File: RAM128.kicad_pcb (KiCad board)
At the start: 4 copper layers, 71.6 x 35.7 mm, 33 parts, among them J1 AppleIIBus, U1 621024, U10 74LS32, U11 74AHC1G126GW, U2 74HCT245, U3 74LS273, U4 74LS273, U5 74LS04, U6 74LS08, U7 74LS08, U8 74LS08, U9 74LS08

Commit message: Update docs
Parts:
- C1: renamed from C13; value 2u2 -> 10u
- C11: renamed from C1; value 2u2 -> 10u
- C12: renamed from C5; value 2u2 -> 10u
- U10: value 74LS32 -> 74HCT32
- U3, U4: value 74LS273 -> 74HCT273
- U5: value 74LS04 -> 74HCT04
- U6, U7, U8, U9: value 74LS08 -> 74HCT08
- renumbered C12 to C10, C3 to C2, C11 to C3, C2 to C4, C6 to C5, C7 to C6, C8 to C7, C9 to C8, C10 to C9, FID5 to FID1, FID1 to FID3, H5 to H1, H1 to H3
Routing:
- net GND: vias 153 -> 154

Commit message: More stitching
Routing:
- net /ENRD: track 39.0 -> 29.8 mm
- net /~RES~: track 68.4 -> 62.8 mm
- net Net-(U10-Pad8): track 27.3 -> 24.6 mm
- net Net-(U10-Pad10): track 42.7 -> 40.0 mm
- net Net-(U10-Pad11): track 15.0 -> 13.9 mm
- net /R~WE~: track 102.2 -> 101.4 mm
- net Net-(U10-Pad9): track 16.6 -> 16.0 mm
- net GND: track 70.3 -> 69.7 mm, vias 154 -> 169

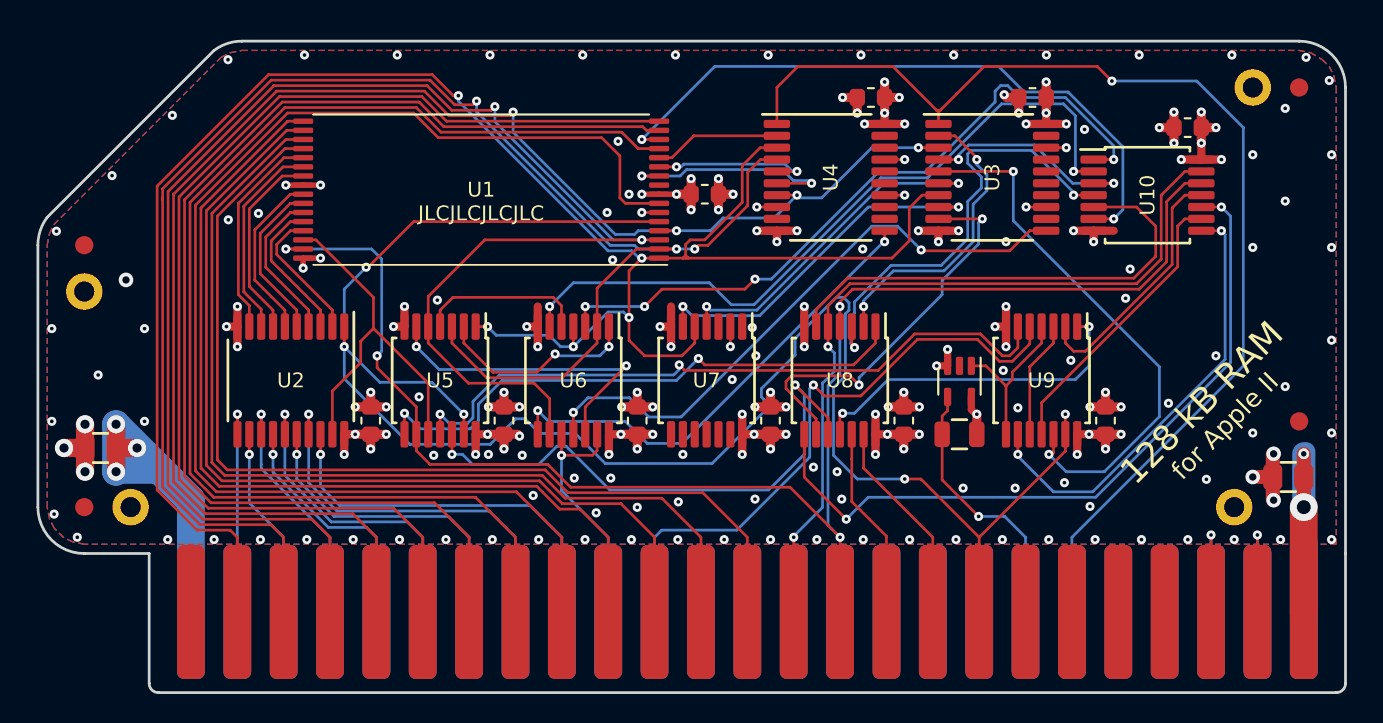
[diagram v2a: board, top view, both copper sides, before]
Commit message: Fixed clock bug
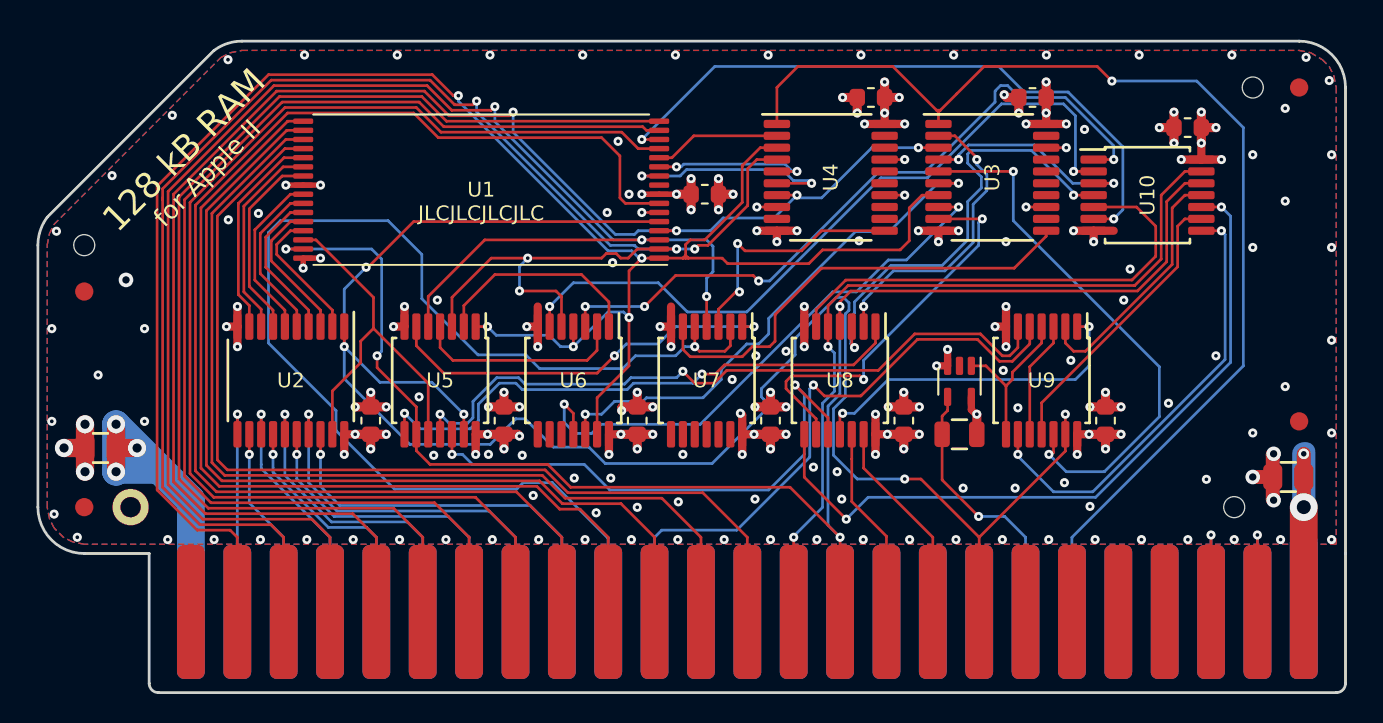
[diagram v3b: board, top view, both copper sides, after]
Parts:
- H2, H3, H4: footprint stdpads:PasteHole_1.1mm_PTH -> stdpads:PasteHole_1.152mm_NPTH
- U11: value 74AHC1G126GW -> 74AHCT1G126GW
- moved FID2 2.54 mm to (70.4, 117.7)
- moved H2 2.54 mm to (70.4, 115.2)
- turned U11 to 90 degrees
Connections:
- U6 pad 10: /~DEVSEL~ -> GND
- U6 pad 11: /~DEV~and~A2~ -> /ENWR1A0
- U6 pad 12: Net-(U5-Pad6) -> /ENWR1
- U6 pad 13: /~DEVSEL~ -> /A0
- U6 pad 2: /A1 -> Net-(U5-Pad4)
- U6 pad 5: Net-(U5-Pad4) -> /A1
- U6 pad 8: /~DEV~andA2 -> Net-(U6-Pad8)
- U6 pad 9: /A2 -> GND
- U7 pad 1: GND -> Net-(U5-Pad6)
- U7 pad 2: GND -> /~DEVSEL~
- U7 pad 3: Net-(U7-Pad3) -> /~DEV~andA2
- U7 pad 4: /ENWR1 -> /A2
- U7 pad 5: /A0 -> /~DEVSEL~
- U7 pad 6: /ENWR1A0 -> /~DEV~and~A2~
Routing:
- net /~DEVSEL~: track 13.7 -> 67.3 mm
- net /~DEV~andA2: track 26.2 -> 13.9 mm
- net /ENWR1A0: track 20.0 -> 31.0 mm
- net /ENWR1: track 19.0 -> 28.8 mm
- net /~DEV~and~A2~: track 33.2 -> 25.2 mm, vias 2 -> 0
- net Net-(U5-Pad6): track 17.9 -> 21.9 mm
- net /A1: track 90.5 -> 93.2 mm, vias 3 -> 5
- net Net-(U5-Pad4): track 9.18 -> 11.6 mm
- net /A2: track 89.2 -> 87.0 mm, vias 2 -> 3
- net /A0: track 108.7 -> 109.7 mm
- net GND: track 69.7 -> 68.8 mm, vias 169 -> 168
- net Net-(U5-Pad12): track 30.3 -> 29.5 mm
- net Net-(U5-Pad2): track 11.3 -> 11.8 mm, vias 2 -> 0

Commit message: Fabbed?
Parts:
- added H5: , stdpads:PasteHole_1.152mm_NPTH, F.Cu at (136.9, 122.3)
- C1: value 10u -> 2u2
- H1: footprint stdpads:PasteHole_1.1mm_PTH -> stdpads:PasteHole_1.152mm_NPTH
- H4: footprint stdpads:PasteHole_1.152mm_NPTH -> stdpads:PasteHole_1.1mm_PTH
- U10: value 74HCT32 -> 74HCT32PW
- U2: value 74HCT245 -> 74HCT245PW
- U3, U4: value 74HCT273 -> 74HCT273PW
- U5: value 74HCT04 -> 74HCT04PW
- U6, U8, U9: value 74HCT08 -> 74HCT08PW
- U7: value 74HCT08 -> 74HCT32PW
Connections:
- net /R~WE~ renamed /R~W~
- net /~DEV~andA2 renamed /A2clk
- net /~DEV~and~A2~ renamed /~A2~clk
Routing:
- net GND: track 68.8 -> 70.8 mm, vias 168 -> 170

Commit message: done with little logic
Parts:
- removed C1, C10, C4, C5, C6, C9: 2u2, stdpads:C_0603
- removed the C2 at (86.0, 124.8)
- removed the C8 at (115.2, 124.8)
- added C2: 2u2, stdpads:C_0603, F.Cu at (92.7, 119.6)
- added C2: 2u2, stdpads:C_0603, F.Cu at (79.1, 120.2)
- added C2: 2u2, stdpads:C_0603, F.Cu at (122.8, 107.0)
- added C2: 2u2, stdpads:C_0603, F.Cu at (105.5, 109.8)
- added C2: 2u2, stdpads:C_0603, F.Cu at (82.8, 114.9)
- added C2: 2u2, stdpads:C_0603, F.Cu at (121.2, 127.0)
- added C2: 2u2, stdpads:C_0603, F.Cu at (114.3, 107.0)
- added C2: 2u2, stdpads:C_0603, F.Cu at (92.7, 127.2)
- added C2: 2u2, stdpads:C_0603, F.Cu at (97.7, 127.2)
- added C8: 2u2, stdpads:C_0603, F.Cu at (83.5, 123.9)
- added C8: 2u2, stdpads:C_0603, F.Cu at (123.5, 122.0)
- added C8: 2u2, stdpads:C_0603, F.Cu at (101.7, 116.0)
- added C8: 2u2, stdpads:C_0603, F.Cu at (113.2, 116.5)
- added C8: 2u2, stdpads:C_0603, F.Cu at (121.8, 116.5)
- added C8: 2u2, stdpads:C_0603, F.Cu at (129.0, 116.8)
- added JP1: Disable DMA Gate, Connector_PinHeader_2.54mm:PinHeader_1x02_P2.54mm_Vertical, F.Cu at (134.4, 116.7)
- added R3: 30, stdpads:R_0603, F.Cu at (133.4, 126.0)
- added R4: 30, stdpads:R_0603, F.Cu at (122.7, 127.0)
- added R6: 3k3, stdpads:R_0603, F.Cu at (131.9, 119.6)
- added U12: 74LVC1G08GW, stdpads:SOT-353, F.Cu at (108.3, 116.5)
- added U13: 74LVC1G32GW, stdpads:SOT-353, F.Cu at (104.3, 116.0)
- added U14: 74LVC1G08GW, stdpads:SOT-353, F.Cu at (108.1, 127.2)
- added U15: 742G04GW, stdpads:SOT-363, F.Cu at (86.8, 127.2)
- added U16: 74LVC1G32GW, stdpads:SOT-353, F.Cu at (124.4, 116.5)
- added U17: 742G04GW, stdpads:SOT-363, F.Cu at (90.2, 127.2)
- added U18: 742G04GW, stdpads:SOT-363, F.Cu at (95.2, 127.2)
- added U19: 74LVC1G08GW, stdpads:SOT-353, F.Cu at (118.1, 122.0)
- added U20: 742G04GW, stdpads:SOT-363, F.Cu at (100.2, 127.2)
- added U21: 74LVC1G32GW, stdpads:SOT-353, F.Cu at (112.9, 122.0)
- added U22: 74LVC1G08GW, stdpads:SOT-353, F.Cu at (130.3, 127.2)
- added U23: 74LVC1G08GW, stdpads:SOT-353, F.Cu at (120.7, 122.0)
- added U24: 74LVC1G08GW, stdpads:SOT-353, F.Cu at (110.3, 122.0)
- added U25: 742G04GW, stdpads:SOT-363, F.Cu at (105.4, 127.2)
- added U26: 74LVC1G08GW, stdpads:SOT-353, F.Cu at (115.9, 127.2)
- added U27: 74LVC1G08GW, stdpads:SOT-353, F.Cu at (127.8, 127.2)
- added U28: 74LVC1G08GW, stdpads:SOT-353, F.Cu at (115.5, 122.0)
- added U29: 742G04GW, stdpads:SOT-363, F.Cu at (113.3, 127.2)
- added U30: 74LVC1G08GW, stdpads:SOT-353, F.Cu at (102.8, 127.2)
- added U31: 742G04GW, stdpads:SOT-363, F.Cu at (102.8, 123.7)
- added U32: 74LVC1G32GW, stdpads:SOT-353, F.Cu at (110.7, 127.2)
- added U33: 742G04GW, stdpads:SOT-363, F.Cu at (118.8, 127.2)
- added U34: 74LVC1G32GW, stdpads:SOT-353, F.Cu at (131.2, 117.0)
- added U35: XC6206PxxxMR, stdpads:SOT-23, F.Cu at (135.9, 123.0)
- R1: footprint stdpads:R_0805 -> stdpads:R_0603
- U1: footprint stdpads:TSOP-I-32_18.4x8mm_P0.5mm -> stdpads:TSOP-I-32_11.8x8mm_P0.5mm
- U10: value 74HCT32PW -> 742G04GW; footprint stdpads:TSSOP-14_4.4x5mm_P0.65mm -> stdpads:SOT-363
- U11: value 74AHCT1G126GW -> 74LVC1G125GW
- U2: value 74HCT245PW -> 74AHC245PW
- U5: value 74HCT04PW -> 74LVC1G08GW; footprint stdpads:TSSOP-14_4.4x5mm_P0.65mm -> stdpads:SOT-353
- U6, U8: value 74HCT08PW -> 74LVC1G32GW; footprint stdpads:TSSOP-14_4.4x5mm_P0.65mm -> stdpads:SOT-353
- U7: value 74HCT32PW -> 74LVC1G08GW; footprint stdpads:TSSOP-14_4.4x5mm_P0.65mm -> stdpads:SOT-353
- U9: value 74HCT08PW -> 74LVC1G08GW; footprint stdpads:TSSOP-14_4.4x5mm_P0.65mm -> stdpads:SOT-353
- moved FID4 105.1 mm to (233.2, 83.0)
- moved U10 51.7 mm to (79.0, 127.2), turned to 90 degrees
- moved U9 38.9 mm to (84.2, 127.2), turned to 270 degrees
- moved U6 31.9 mm to (126.4, 109.8), turned to 0 degrees
- moved U7 23.3 mm to (81.6, 127.2), turned to 270 degrees
- moved C3 18.6 mm to (135.9, 119.7), turned to 0 degrees
- moved U2 12.5 mm to (85.0, 110.5), turned to 90 degrees
- moved H5 11.1 mm to (129.0, 130.2)
- moved U5 10.9 mm to (79.0, 122.9), turned to 270 degrees
- moved U8 7.42 mm to (115.9, 116.5), turned to 0 degrees
- moved U11 7.01 mm to (124.8, 125.4)
- moved R1 6.92 mm to (124.8, 128.1)
- moved U1 5.30 mm to (97.0, 110.2)
- moved C7 2.91 mm to (108.2, 121.9), turned to 270 degrees
- moved U4 0.86 mm to (112.1, 111.4)
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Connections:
- C3 pad 1: +5V -> +3V3
- C7 pad 1: +5V -> +3V3
- J1 pad 24: /DMAin -> /DMAout
- R1 pad 1: +5V -> +3V3
- R1 pad 2: /~INH~ -> Net-(R1-Pad2)
- U1 pad 1: /A0 -> /RA12
- U1 pad 10: /RA16 -> /~A8
- U1 pad 11: /RA15 -> /~A7
- U1 pad 12: /RA14 -> /~A6
- U1 pad 13: /A6 -> /~A5
- U1 pad 14: /RA12 -> /RA16
- U1 pad 15: /A5 -> /RA15
- U1 pad 16: /A4 -> /RA14
- U1 pad 17: /A8 -> /~A4
- U1 pad 18: /A9 -> /~A3
- U1 pad 19: /A10 -> /~A2
- U1 pad 2: /A1 -> /RA13
- U1 pad 20: /A11 -> /~A1
- U1 pad 3: /A2 -> /~A11
- U1 pad 31: /A13 -> /~A0
- U1 pad 4: /A3 -> /~A10
- U1 pad 5: /R~W~ -> /RR~W~
- U1 pad 6: +5V -> +3V3
- U1 pad 7: /A7 -> /~A9
- U1 pad 8: +5V -> +3V3
- U10 pad 1: Net-(U10-Pad1) -> /A0
- U10 pad 2: Net-(U10-Pad2) -> GND
- U10 pad 3: /~A0XOR1~ -> /A1
- U10 pad 4: Net-(U10-Pad4) -> /~A1
- U10 pad 5: Net-(U10-Pad5) -> +3V3
- U10 pad 6: /RA12 -> /~A0
- U11 pad 1: /INHOE -> /~INHOE~
- U11 pad 4: /~INH~ -> Net-(R1-Pad2)
- U11 pad 5: +5V -> +3V3
- U2 pad 1: /R~W~ -> /RR~W~
- U2 pad 20: +5V -> +3V3
- U3 pad 17: GND -> +3V3
- U3 pad 20: +5V -> +3V3
- U4 pad 20: +5V -> +3V3
- U5 pad 1: /A0 -> /~A0
- U5 pad 2: Net-(U5-Pad2) -> /~A1
- U5 pad 3: /A1 -> GND
- U5 pad 5: /A2 -> +3V3
- U6 pad 1: Net-(U5-Pad2) -> Net-(U6-Pad1)
- U6 pad 3: Net-(U10-Pad1) -> GND
- U6 pad 4: /A0 -> /~A0XOR1~
- U6 pad 5: /A1 -> +3V3
- U7 pad 1: Net-(U5-Pad6) -> /A0
- U7 pad 2: /~DEVSEL~ -> /A1
- U7 pad 3: /A2clk -> GND
- U7 pad 4: /A2 -> Net-(U6-Pad1)
- U7 pad 5: /~DEVSEL~ -> +3V3
- U8 pad 1: Net-(U5-Pad8) -> /~A2
- U8 pad 2: /BankAB -> /~DEVSEL~
- U8 pad 3: Net-(U10-Pad4) -> GND
- U8 pad 4: /A13 -> /A2clk
- U8 pad 5: /A12 -> +3V3
- U9 pad 1: Net-(U8-Pad11) -> /ENWR1
- U9 pad 2: Net-(U10-Pad11) -> /A0
- U9 pad 3: Net-(U9-Pad10) -> GND
- U9 pad 4: /INHOE -> /ENWR1A0
- U9 pad 5: /PHI0 -> +3V3
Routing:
- net /R~W~: track 101.4 -> 7.24 mm, vias 5 -> 0
- net +3V3: track 0.00 -> 89.2 mm, vias 0 -> 87
- net Net-(U6-Pad1): track 0.00 -> 74.8 mm, vias 0 -> 2
- net /A13: track 86.2 -> 12.0 mm, vias 4 -> 2
- net /A7: track 71.1 -> 7.49 mm
- net Net-(U5-Pad4): track 11.6 -> 73.7 mm, vias 0 -> 2
- net /A6: track 67.0 -> 7.49 mm
- net /A5: track 65.1 -> 7.50 mm
- net /~A2: track 0.00 -> 56.2 mm, vias 0 -> 2
- net /A4: track 63.4 -> 7.48 mm
- net /RR~W~: track 0.00 -> 51.5 mm, vias 0 -> 3
- net /A11: track 54.5 -> 7.49 mm
- net /~INHOE~: track 0.00 -> 45.5 mm, vias 0 -> 2
- net /A10: track 52.9 -> 7.48 mm
- net /A9: track 51.3 -> 7.54 mm
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- added copper zone on In2.Cu, net +3V3
- removed copper zone on In2.Cu, net +5V
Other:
- board text removed: "JLCJLCJLCJLC"

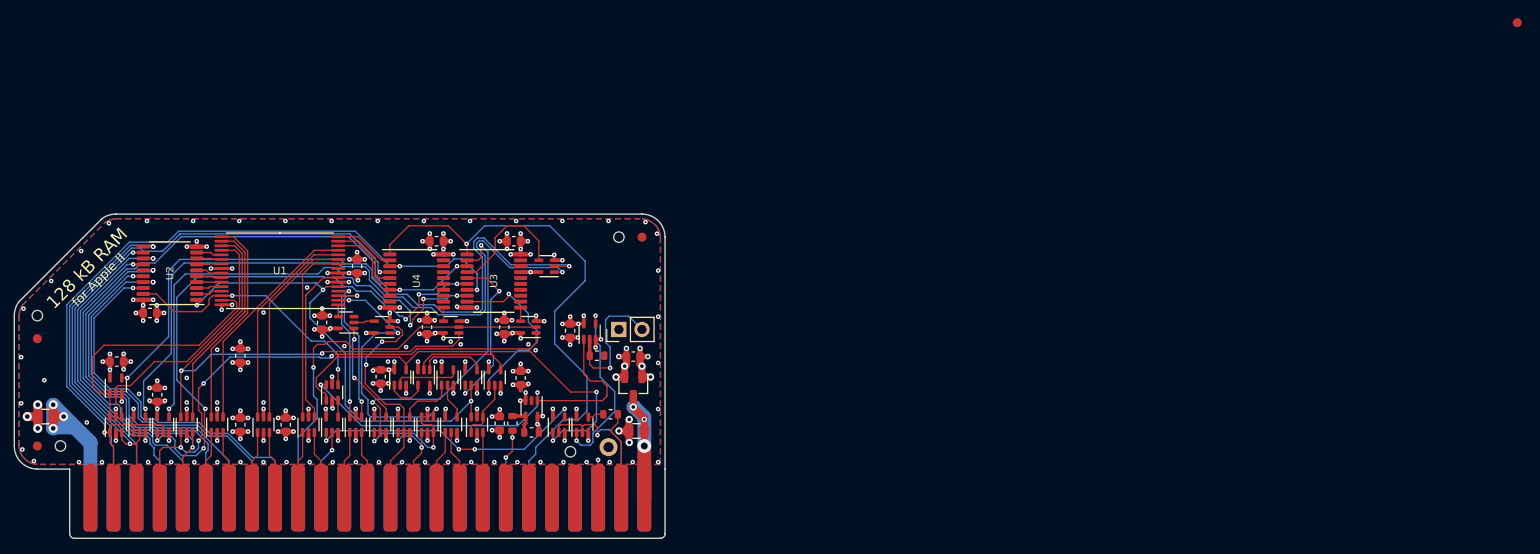
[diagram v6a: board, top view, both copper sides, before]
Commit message: Revert "done with little logic"
This reverts commit 34a57e67dbc9bf65fa4ad86b3c90b017081c5d83.
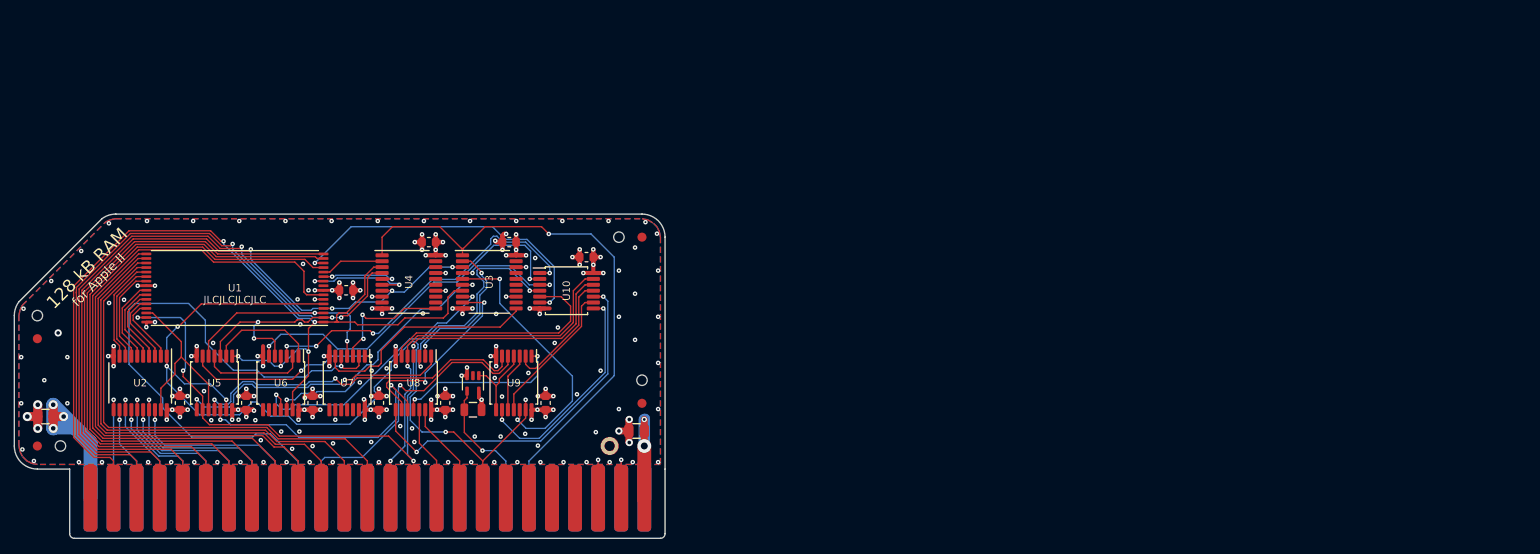
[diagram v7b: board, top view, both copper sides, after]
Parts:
- removed the C2 at (92.7, 119.6)
- removed the C2 at (79.1, 120.2)
- removed the C2 at (122.8, 107.0)
- removed the C2 at (105.5, 109.8)
- removed the C2 at (82.8, 114.9)
- removed the C2 at (121.2, 127.0)
- removed the C2 at (114.3, 107.0)
- removed the C2 at (92.7, 127.2)
- removed the C2 at (97.7, 127.2)
- removed the C8 at (83.5, 123.9)
- removed the C8 at (123.5, 122.0)
- removed the C8 at (101.7, 116.0)
- removed the C8 at (113.2, 116.5)
- removed the C8 at (121.8, 116.5)
- removed the C8 at (129.0, 116.8)
- removed JP1: Disable DMA Gate, Connector_PinHeader_2.54mm:PinHeader_1x02_P2.54mm_Vertical
- removed R3, R4: 30, stdpads:R_0603
- removed R6: 3k3, stdpads:R_0603
- removed U12, U14, U19, U22, U23, U24, U26, U27, U28, U30: 74LVC1G08GW, stdpads:SOT-353
- removed U13, U16, U21, U32, U34: 74LVC1G32GW, stdpads:SOT-353
- removed U15, U17, U18, U20, U25, U29, U31, U33: 742G04GW, stdpads:SOT-363
- removed U35: XC6206PxxxMR, stdpads:SOT-23
- added C1: 2u2, stdpads:C_0603, F.Cu at (104.3, 112.4)
- added C10: 2u2, stdpads:C_0603, F.Cu at (130.8, 108.8)
- added C2: 2u2, stdpads:C_0603, F.Cu at (86.0, 124.8)
- added C4: 2u2, stdpads:C_0603, F.Cu at (113.5, 107.1)
- added C5: 2u2, stdpads:C_0603, F.Cu at (93.3, 124.8)
- added C6: 2u2, stdpads:C_0603, F.Cu at (100.7, 124.8)
- added C8: 2u2, stdpads:C_0603, F.Cu at (115.2, 124.8)
- added C9: 2u2, stdpads:C_0603, F.Cu at (126.3, 124.8)
- R1: footprint stdpads:R_0603 -> stdpads:R_0805
- U1: footprint stdpads:TSOP-I-32_11.8x8mm_P0.5mm -> stdpads:TSOP-I-32_18.4x8mm_P0.5mm
- U10: value 742G04GW -> 74HCT32PW; footprint stdpads:SOT-363 -> stdpads:TSSOP-14_4.4x5mm_P0.65mm
- U11: value 74LVC1G125GW -> 74AHCT1G126GW
- U2: value 74AHC245PW -> 74HCT245PW
- U5: value 74LVC1G08GW -> 74HCT04PW; footprint stdpads:SOT-353 -> stdpads:TSSOP-14_4.4x5mm_P0.65mm
- U6, U8: value 74LVC1G32GW -> 74HCT08PW; footprint stdpads:SOT-353 -> stdpads:TSSOP-14_4.4x5mm_P0.65mm
- U7: value 74LVC1G08GW -> 74HCT32PW; footprint stdpads:SOT-353 -> stdpads:TSSOP-14_4.4x5mm_P0.65mm
- U9: value 74LVC1G08GW -> 74HCT08PW; footprint stdpads:SOT-353 -> stdpads:TSSOP-14_4.4x5mm_P0.65mm
- moved FID4 105.1 mm to (136.9, 124.8)
- moved U10 51.7 mm to (128.6, 112.5), turned to 270 degrees
- moved U9 38.9 mm to (122.8, 122.6), turned to 180 degrees
- moved U6 31.9 mm to (97.2, 122.6), turned to 180 degrees
- moved U7 23.3 mm to (104.5, 122.6), turned to 180 degrees
- moved C3 18.6 mm to (122.3, 107.1), turned to 180 degrees
- moved U2 12.5 mm to (81.7, 122.6), turned to 180 degrees
- moved H5 11.1 mm to (136.9, 122.3)
- moved U5 10.9 mm to (89.8, 122.6), turned to 180 degrees
- moved U8 7.42 mm to (111.8, 122.6), turned to 180 degrees
- moved U11 7.01 mm to (118.3, 122.7)
- moved R1 6.92 mm to (118.3, 125.5)
- moved U1 5.30 mm to (92.1, 112.2)
- moved C7 2.91 mm to (108.0, 124.8), turned to 90 degrees
- moved U4 0.86 mm to (111.2, 111.5)
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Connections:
- C3 pad 1: +3V3 -> +5V
- C7 pad 1: +3V3 -> +5V
- J1 pad 24: /DMAout -> /DMAin
- R1 pad 1: +3V3 -> +5V
- R1 pad 2: Net-(R1-Pad2) -> /~INH~
- U1 pad 1: /RA12 -> /A0
- U1 pad 10: /~A8 -> /RA16
- U1 pad 11: /~A7 -> /RA15
- U1 pad 12: /~A6 -> /RA14
- U1 pad 13: /~A5 -> /A6
- U1 pad 14: /RA16 -> /RA12
- U1 pad 15: /RA15 -> /A5
- U1 pad 16: /RA14 -> /A4
- U1 pad 17: /~A4 -> /A8
- U1 pad 18: /~A3 -> /A9
- U1 pad 19: /~A2 -> /A10
- U1 pad 2: /RA13 -> /A1
- U1 pad 20: /~A1 -> /A11
- U1 pad 3: /~A11 -> /A2
- U1 pad 31: /~A0 -> /A13
- U1 pad 4: /~A10 -> /A3
- U1 pad 5: /RR~W~ -> /R~W~
- U1 pad 6: +3V3 -> +5V
- U1 pad 7: /~A9 -> /A7
- U1 pad 8: +3V3 -> +5V
- U10 pad 1: /A0 -> Net-(U10-Pad1)
- U10 pad 2: GND -> Net-(U10-Pad2)
- U10 pad 3: /A1 -> /~A0XOR1~
- U10 pad 4: /~A1 -> Net-(U10-Pad4)
- U10 pad 5: +3V3 -> Net-(U10-Pad5)
- U10 pad 6: /~A0 -> /RA12
- U11 pad 1: /~INHOE~ -> /INHOE
- U11 pad 4: Net-(R1-Pad2) -> /~INH~
- U11 pad 5: +3V3 -> +5V
- U2 pad 1: /RR~W~ -> /R~W~
- U2 pad 20: +3V3 -> +5V
- U3 pad 17: +3V3 -> GND
- U3 pad 20: +3V3 -> +5V
- U4 pad 20: +3V3 -> +5V
- U5 pad 1: /~A0 -> /A0
- U5 pad 2: /~A1 -> Net-(U5-Pad2)
- U5 pad 3: GND -> /A1
- U5 pad 5: +3V3 -> /A2
- U6 pad 1: Net-(U6-Pad1) -> Net-(U5-Pad2)
- U6 pad 3: GND -> Net-(U10-Pad1)
- U6 pad 4: /~A0XOR1~ -> /A0
- U6 pad 5: +3V3 -> /A1
- U7 pad 1: /A0 -> Net-(U5-Pad6)
- U7 pad 2: /A1 -> /~DEVSEL~
- U7 pad 3: GND -> /A2clk
- U7 pad 4: Net-(U6-Pad1) -> /A2
- U7 pad 5: +3V3 -> /~DEVSEL~
- U8 pad 1: /~A2 -> Net-(U5-Pad8)
- U8 pad 2: /~DEVSEL~ -> /BankAB
- U8 pad 3: GND -> Net-(U10-Pad4)
- U8 pad 4: /A2clk -> /A13
- U8 pad 5: +3V3 -> /A12
- U9 pad 1: /ENWR1 -> Net-(U8-Pad11)
- U9 pad 2: /A0 -> Net-(U10-Pad11)
- U9 pad 3: GND -> Net-(U9-Pad10)
- U9 pad 4: /ENWR1A0 -> /INHOE
- U9 pad 5: +3V3 -> /PHI0
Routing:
- net /R~W~: track 7.24 -> 101.4 mm, vias 0 -> 5
- net +3V3: track 89.2 -> 0.00 mm, vias 87 -> 0
- net Net-(U6-Pad1): track 74.8 -> 0.00 mm, vias 2 -> 0
- net /A13: track 12.0 -> 86.2 mm, vias 2 -> 4
- net /A7: track 7.49 -> 71.1 mm
- net Net-(U5-Pad4): track 73.7 -> 11.6 mm, vias 2 -> 0
- net /A6: track 7.49 -> 67.0 mm
- net /A5: track 7.50 -> 65.1 mm
- net /~A2: track 56.2 -> 0.00 mm, vias 2 -> 0
- net /A4: track 7.48 -> 63.4 mm
- net /RR~W~: track 51.5 -> 0.00 mm, vias 3 -> 0
- net /A11: track 7.49 -> 54.5 mm
- net /~INHOE~: track 45.5 -> 0.00 mm, vias 2 -> 0
- net /A10: track 7.48 -> 52.9 mm
- net /A9: track 7.54 -> 51.3 mm
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- added copper zone on In2.Cu, net +5V
- removed copper zone on In2.Cu, net +3V3
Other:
- board text added: "JLCJLCJLCJLC"
